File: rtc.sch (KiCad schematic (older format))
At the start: 3 parts, among them U4 DS3231MZ

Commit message: Add LCSC part numbers to components
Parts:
- C27: LCSC (none) -> C14663
- U4: LCSC (none) -> C107410
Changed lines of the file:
@@
 F 2 "Capacitor_SMD:C_0603_1608Metric_Pad1.05x0.95mm_HandSolder" H 2988 1200 50  0001 C CNN
 F 3 "~" H 2950 1350 50  0001 C CNN
+F 4 "C14663" H 2950 1350 50  0001 C CNN "LCSC"
 	1    2950 1350
 	0    -1   -1   0
@@
 F 2 "Package_SO:SOIC-8_3.9x4.9mm_P1.27mm" H 2600 1650 50  0001 C CNN
 F 3 "http://datasheets.maximintegrated.com/en/ds/DS3231M.pdf" H 2600 1550 50  0001 C CNN
+F 4 "C107410" H 2600 2150 50  0001 C CNN "LCSC"
 	1    2600 2150
 	1    0    0    -1

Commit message: Isolated CAN bus implementation
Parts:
- C27: footprint Capacitor_SMD:C_0603_1608Metric_Pad1.05x0.95mm_HandSolder -> Capacitor_SMD:C_0603_1608Metric
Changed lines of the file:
@@
 $Descr A4 11693 8268
 encoding utf-8
-Sheet 6 7
+Sheet 5 7
 Title ""
 Date ""
@@
 F 0 "C27" H 3065 1396 50  0000 L CNN
 F 1 "100nF" H 3065 1305 50  0000 L CNN
-F 2 "Capacitor_SMD:C_0603_1608Metric_Pad1.05x0.95mm_HandSolder" H 2988 1200 50  0001 C CNN
+F 2 "Capacitor_SMD:C_0603_1608Metric" H 2988 1200 50  0001 C CNN
 F 3 "~" H 2950 1350 50  0001 C CNN
 F 4 "C14663" H 2950 1350 50  0001 C CNN "LCSC"

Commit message: Parts updated to match JLCPCB availability
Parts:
- BT1: Mouser (none) -> 712-BAT-HLD-012-SMT
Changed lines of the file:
@@
 F 2 "custom:BatteryHolder_Linx_BAT-HLD-012-SMT" V 3550 2360 50  0001 C CNN
 F 3 "~" V 3550 2360 50  0001 C CNN
+F 4 "712-BAT-HLD-012-SMT" H 3550 2300 50  0001 C CNN "Mouser"
 	1    3550 2300
 	1    0    0    -1

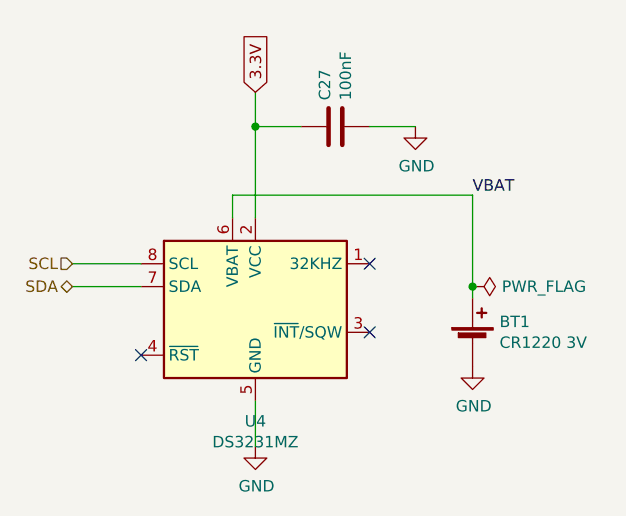
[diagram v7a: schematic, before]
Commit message: Schema updated
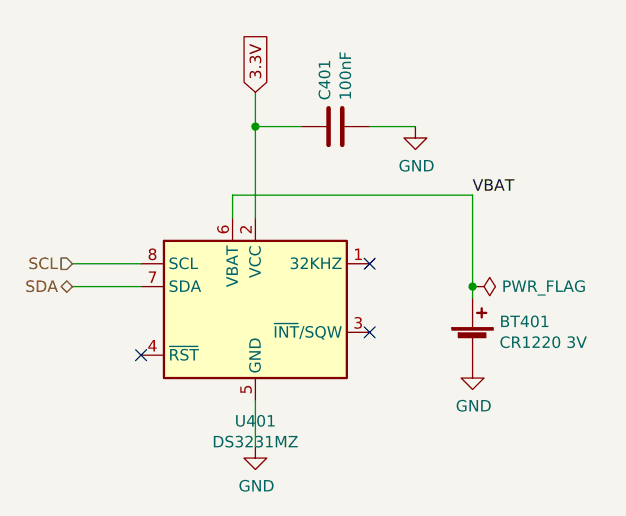
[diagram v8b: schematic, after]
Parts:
- renumbered BT1 to BT401, C27 to C401, U4 to U401
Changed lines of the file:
@@
 $Descr A4 11693 8268
 encoding utf-8
-Sheet 5 7
-Title ""
+Sheet 5 8
+Title "Sailor Hat for Raspberry Pi"
 Date ""
-Rev ""
-Comp ""
-Comment1 ""
-Comment2 ""
-Comment3 ""
+Rev "revL"
+Comp "Hat Laboratories"
+Comment1 "https://creativecommons.org/licenses/by-sa/4.0"
+Comment2 "To view a copy of this license, visit "
+Comment3 "Sailor Hat for ESP32 is licensed under CC BY-SA 4.0."
 Comment4 ""
 $EndDescr
 $Comp
-L Device:C C27
+L Device:C C401
 U 1 1 5C353CB0
 P 2950 1350
-F 0 "C27" H 3065 1396 50  0000 L CNN
+F 0 "C401" H 3065 1396 50  0000 L CNN
 F 1 "100nF" H 3065 1305 50  0000 L CNN
 F 2 "Capacitor_SMD:C_0603_1608Metric" H 2988 1200 50  0001 C CNN
@@
 3.3V
 $Comp
-L power:GND #PWR035
+L power:GND #PWR0402
 U 1 1 5C354469
 P 3300 1350
-F 0 "#PWR035" H 3300 1100 50  0001 C CNN
+F 0 "#PWR0402" H 3300 1100 50  0001 C CNN
 F 1 "GND" H 3305 1177 50  0000 C CNN
 F 2 "" H 3300 1350 50  0001 C CNN
@@
 	1800 2050 2100 2050
 $Comp
-L power:GND #PWR034
+L power:GND #PWR0401
 U 1 1 5C35498E
 P 2600 2750
-F 0 "#PWR034" H 2600 2500 50  0001 C CNN
+F 0 "#PWR0401" H 2600 2500 50  0001 C CNN
 F 1 "GND" H 2605 2577 50  0000 C CNN
 F 2 "" H 2600 2750 50  0001 C CNN
@@
 	2600 2750 2600 2550
 $Comp
-L Device:Battery_Cell BT1
+L Device:Battery_Cell BT401
 U 1 1 5C354C49
 P 3550 2300
-F 0 "BT1" H 3668 2396 50  0000 L CNN
+F 0 "BT401" H 3668 2396 50  0000 L CNN
 F 1 "CR1220 3V" H 3668 2305 50  0000 L CNN
 F 2 "custom:BatteryHolder_Linx_BAT-HLD-012-SMT" V 3550 2360 50  0001 C CNN
@@
 $EndComp
 $Comp
-L power:GND #PWR036
+L power:GND #PWR0403
 U 1 1 5C354D0D
 P 3550 2400
-F 0 "#PWR036" H 3550 2150 50  0001 C CNN
+F 0 "#PWR0403" H 3550 2150 50  0001 C CNN
 F 1 "GND" H 3555 2227 50  0000 C CNN
 F 2 "" H 3550 2400 50  0001 C CNN
@@
 NoConn ~ 3100 1950
 $Comp
-L power:PWR_FLAG #FLG07
+L power:PWR_FLAG #FLG0401
 U 1 1 5C392B36
 P 3550 2050
-F 0 "#FLG07" H 3550 2125 50  0001 C CNN
+F 0 "#FLG0401" H 3550 2125 50  0001 C CNN
 F 1 "PWR_FLAG" V 3550 2178 50  0000 L CNN
 F 2 "" H 3550 2050 50  0001 C CNN
@@
 VBAT
 $Comp
-L Timer_RTC:DS3231MZ U4
+L Timer_RTC:DS3231MZ U401
 U 1 1 5D77B733
 P 2600 2150
-F 0 "U4" H 2600 1661 50  0000 C CNN
+F 0 "U401" H 2600 1661 50  0000 C CNN
 F 1 "DS3231MZ" H 2600 1570 50  0000 C CNN
 F 2 "Package_SO:SOIC-8_3.9x4.9mm_P1.27mm" H 2600 1650 50  0001 C CNN
